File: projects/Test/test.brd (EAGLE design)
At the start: 65.8 x 27.6 mm, 48 parts, among them J1 284512-3, Y1 ECS-80-S-4X

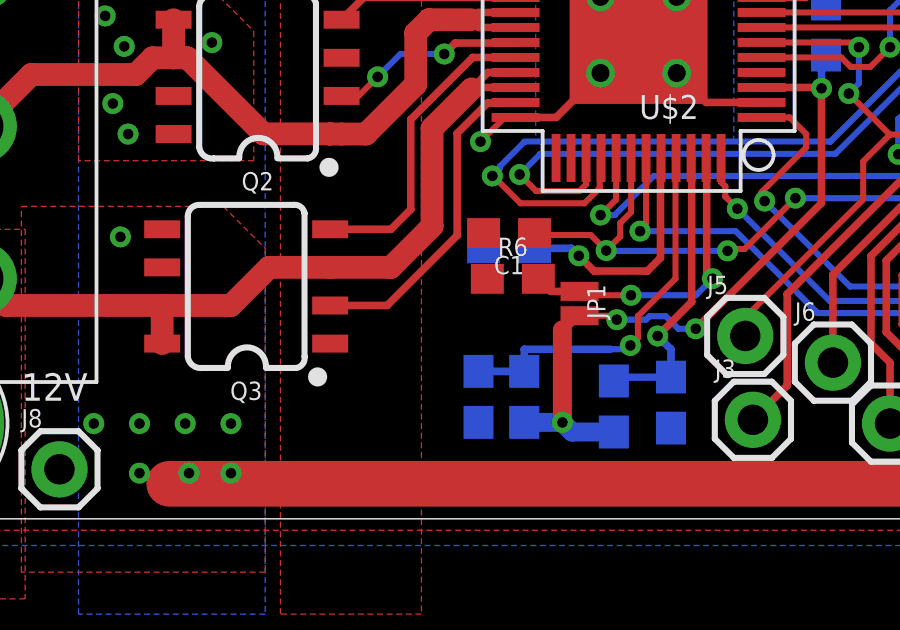
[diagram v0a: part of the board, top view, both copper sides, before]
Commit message: fixed airwires
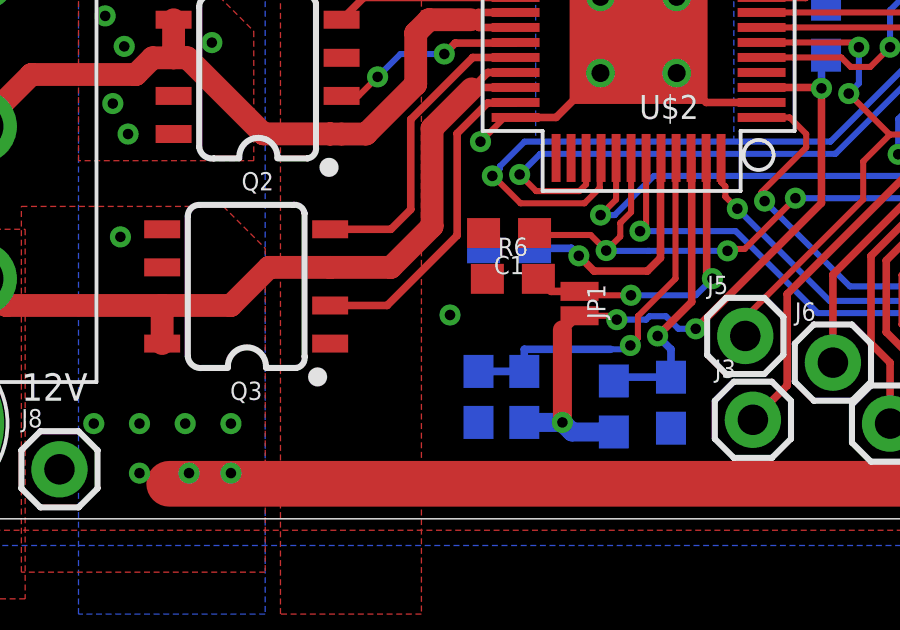
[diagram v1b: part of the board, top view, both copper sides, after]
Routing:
- net GND: vias 13 -> 14
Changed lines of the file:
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@@
 <layer number="43" name="vRestrict" color="2" fill="10" visible="yes" active="yes"/>
 <layer number="44" name="Drills" color="7" fill="1" visible="no" active="yes"/>
-<layer number="45" name="Holes" color="7" fill="1" visible="no" active="yes"/>
+<layer number="45" name="Holes" color="7" fill="1" visible="yes" active="yes"/>
 <layer number="46" name="Milling" color="3" fill="1" visible="no" active="yes"/>
 <layer number="47" name="Measures" color="7" fill="1" visible="no" active="yes"/>
@@
 <wire x1="38.543" y1="17.1541" x2="38.5445" y2="17.1556" width="0.2032" layer="1"/>
 <via x="38.5445" y="17.1556" extent="1-16" drill="0.35"/>
+<via x="20.8915" y="6.4135" extent="1-16" drill="0.35"/>
 <wire x1="27.178" y1="15.748" x2="28.448" y2="14.478" width="0" layer="19" extent="1-1"/>
 <wire x1="27.178" y1="15.748" x2="27.178" y2="15.748" width="0" layer="19" extent="1-16"/>
-<wire x1="22.01" y1="9.144" x2="22.01" y2="8.636" width="0" layer="19" extent="1-16"/>
 <wire x1="25.908" y1="17.018" x2="27.178" y2="15.748" width="0" layer="19" extent="1-1"/>
 </signal>

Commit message: updated board
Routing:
- net SOB: track 31.3 -> 0.06 mm, vias 2 -> 0
- net SOC: track 26.0 -> 0.00 mm, vias 2 -> 0
- net SOA: track 23.2 -> 0.00 mm, vias 2 -> 0
- net GND: track 23.5 -> 28.8 mm, vias 14 -> 19
- net PHASE_B1: track 28.4 -> 27.6 mm
- net 12V: vias 14 -> 16
- added copper zone on layer 1, net PHASE_A1
- added copper zone on layer 1, net PHASE_B1

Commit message: Final touches before ordering
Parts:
- added R12: 10k, SparkFun-Resistors:0603
- R4: value 1k -> 10k
- moved J9 0.70 mm to (8.57, 22.8)
- moved R7 0.26 mm to (22.8, 8.38)
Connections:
- new net N$2: U$5.15
- new net N$3: U$5.14
- new net N$4: U$5.29
- net +3V3: now also R12.2
- net FAULT_1: now also R12.1
- net N$1: no longer U$5.29
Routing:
- net GND: track 28.8 -> 32.0 mm, vias 19 -> 36
- net SOC: track 0.00 -> 3.11 mm, vias 0 -> 1
- net 12V: track 102.8 -> 99.8 mm, vias 16 -> 23
- net FAULT_1: track 18.3 -> 21.1 mm
- net +3V3: track 47.6 -> 50.0 mm
- net N$4: track 0.00 -> 1.90 mm, vias 0 -> 1
- net SOA: track 0.00 -> 1.84 mm, vias 0 -> 1
- net SOB: track 0.06 -> 1.86 mm, vias 0 -> 1
- net CAL: track 15.6 -> 13.8 mm
- net PHASE_B1: track 27.6 -> 29.1 mm
- net N$1: track 0.00 -> 1.47 mm, vias 0 -> 1
- net SWCLK: track 38.9 -> 38.2 mm
- net INHB_1: track 23.0 -> 22.3 mm
- removed copper zone on layer 1, net PHASE_A1
- removed copper zone on layer 1, net PHASE_B1
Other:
- board text added: "12V - 12V - GND - NRST -SWDIO- GND -SWCLK- 3V3"
- board text added: "Custom ESC Test board v2 Kaitlyn Yu Justin Zhang Grant Geyer Read Hedl Mar 20, 2021"
- board text added: "HA"
- board text added: "HB LA"
- board text added: "HC LC"
- board text added: "LB"
- board text added: "RX - TX"

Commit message: Final changes before ordering
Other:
- board text added: "Custom ESC Test board v2 Kaitlyn Yu Grant Geyer Read Hedl Mar 20, 2021"
- board text removed: "Custom ESC Test board v2 Kaitlyn Yu Justin Zhang Grant Geyer Read Hedl Mar 20, 2021"
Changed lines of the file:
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@@
 <text x="46.0375" y="0.508" size="0.508" layer="25">Custom ESC Test board v2
 Kaitlyn Yu
-Justin Zhang
 Grant Geyer
 Read Hedl
@@
 <wire x1="11.678" y1="15.875" x2="11.1065" y2="15.3035" width="1.27" layer="1"/>
 <wire x1="11.678" y1="14.986" x2="11.678" y2="16.256" width="1.27" layer="1"/>
-<wire x1="11.678" y1="14.986" x2="11.8098" y2="14.8542" width="1.27" layer="1"/>
-<wire x1="11.8098" y1="14.8542" x2="13.76819375" y2="14.8542" width="1.27" layer="1"/>
+<wire x1="13.57769375" y1="15.0447" x2="11.7367" y2="15.0447" width="1.27" layer="1"/>
+<wire x1="11.678" y1="14.986" x2="11.7367" y2="15.0447" width="1.27" layer="1"/>
 <wire x1="16.17639375" y1="12.446" x2="17.278" y2="12.446" width="1.27" layer="1"/>
-<wire x1="13.76819375" y1="14.8542" x2="16.17639375" y2="12.446" width="1.27" layer="1"/>
+<wire x1="13.57769375" y1="15.0447" x2="16.17639375" y2="12.446" width="1.27" layer="1"/>
 <wire x1="21.59" y1="16.256" x2="20.701" y2="16.256" width="0.2032" layer="1"/>
 <wire x1="20.701" y1="16.256" x2="19.8755" y2="15.4305" width="0.2032" layer="1"/>
@@
 <wire x1="7.366" y1="5.461" x2="11.297" y2="5.461" width="1.778" layer="1"/>
 <wire x1="11.297" y1="5.461" x2="11.297" y2="6.731" width="1.27" layer="1"/>
-<wire x1="11.297" y1="6.731" x2="11.4288" y2="6.8628" width="1.27" layer="1"/>
-<wire x1="11.4288" y1="6.8628" x2="12.24419375" y2="6.8628" width="1.27" layer="1"/>
-<wire x1="13.38239375" y1="8.001" x2="16.897" y2="8.001" width="1.27" layer="1"/>
-<wire x1="12.24419375" y1="6.8628" x2="13.38239375" y2="8.001" width="1.27" layer="1"/>
+<wire x1="11.297" y1="6.731" x2="11.3018" y2="6.7358" width="1.27" layer="1"/>
+<wire x1="11.3018" y1="6.7358" x2="12.87919375" y2="6.7358" width="1.27" layer="1"/>
+<wire x1="14.14439375" y1="8.001" x2="16.897" y2="8.001" width="1.27" layer="1"/>
+<wire x1="12.87919375" y1="6.7358" x2="14.14439375" y2="8.001" width="1.27" layer="1"/>
 <wire x1="18.6055" y1="8.001" x2="16.897" y2="8.001" width="0.254" layer="1"/>
 <wire x1="21.862615625" y1="14.205384375" x2="20.3835" y2="12.72626875" width="0.254" layer="1"/>

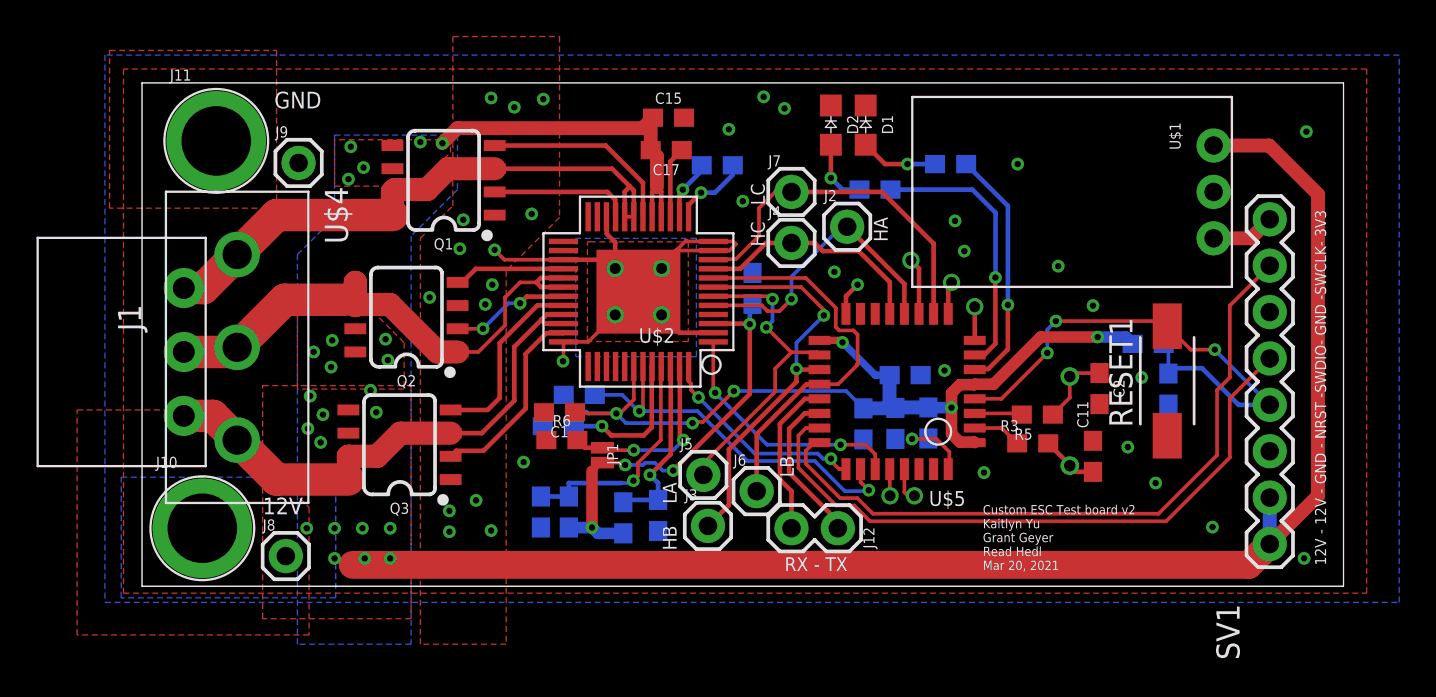
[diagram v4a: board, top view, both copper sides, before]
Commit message: Switch PWM lines to be optimized for 3x PWM
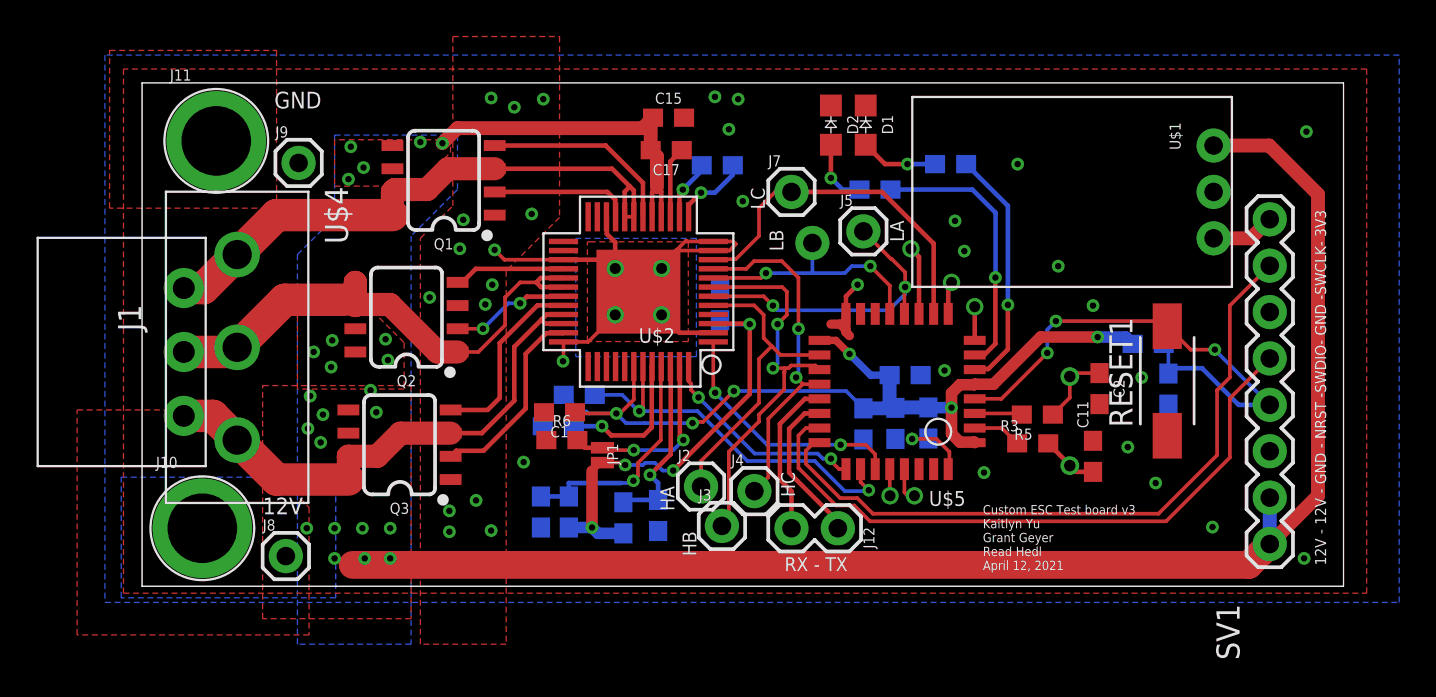
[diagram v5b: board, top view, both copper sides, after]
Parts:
- moved J2 16.3 mm to (30.6, 5.08)
- moved J5 16.0 mm to (39.5, 19.1)
- moved J6 13.9 mm to (36.7, 18.4), flipped to the bottom
- moved J4 13.7 mm to (33.5, 4.83)
- moved C14 1.99 mm to (31.6, 15.0)
- moved J3 0.76 mm to (31.8, 2.92)
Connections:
- net INHA_1: now also U$5.18; no longer U$5.12
- net INHC_1: now also U$5.20; no longer U$5.13
- net INLA_1: now also U$5.12; no longer U$5.18
- net INLB_1: now also U$5.13; no longer U$5.20
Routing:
- net INLB_1: track 21.8 -> 13.6 mm, vias 0 -> 2
- net INHC_1: track 12.9 -> 19.1 mm, vias 0 -> 2
- net GND: track 32.0 -> 34.3 mm, vias 36 -> 35
- net INHB_1: track 22.3 -> 21.4 mm
- net INHA_1: track 16.2 -> 17.0 mm, vias 1 -> 0
- net SOC: track 3.11 -> 3.75 mm
- net 3V3_OUT: track 24.0 -> 24.6 mm
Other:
- board text added: "Custom ESC Test board v3 Kaitlyn Yu Grant Geyer Read Hedl April 12, 2021"
- board text added: "HB"
- board text added: "HC"
- board text added: "LA"
- board text added: "LC"
- board text removed: "Custom ESC Test board v2 Kaitlyn Yu Grant Geyer Read Hedl Mar 20, 2021"
- board text removed: "HB LA"
- board text removed: "HC LC"
